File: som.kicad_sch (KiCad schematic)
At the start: 31 parts, among them M2 jetson-orin-nx/nano-module

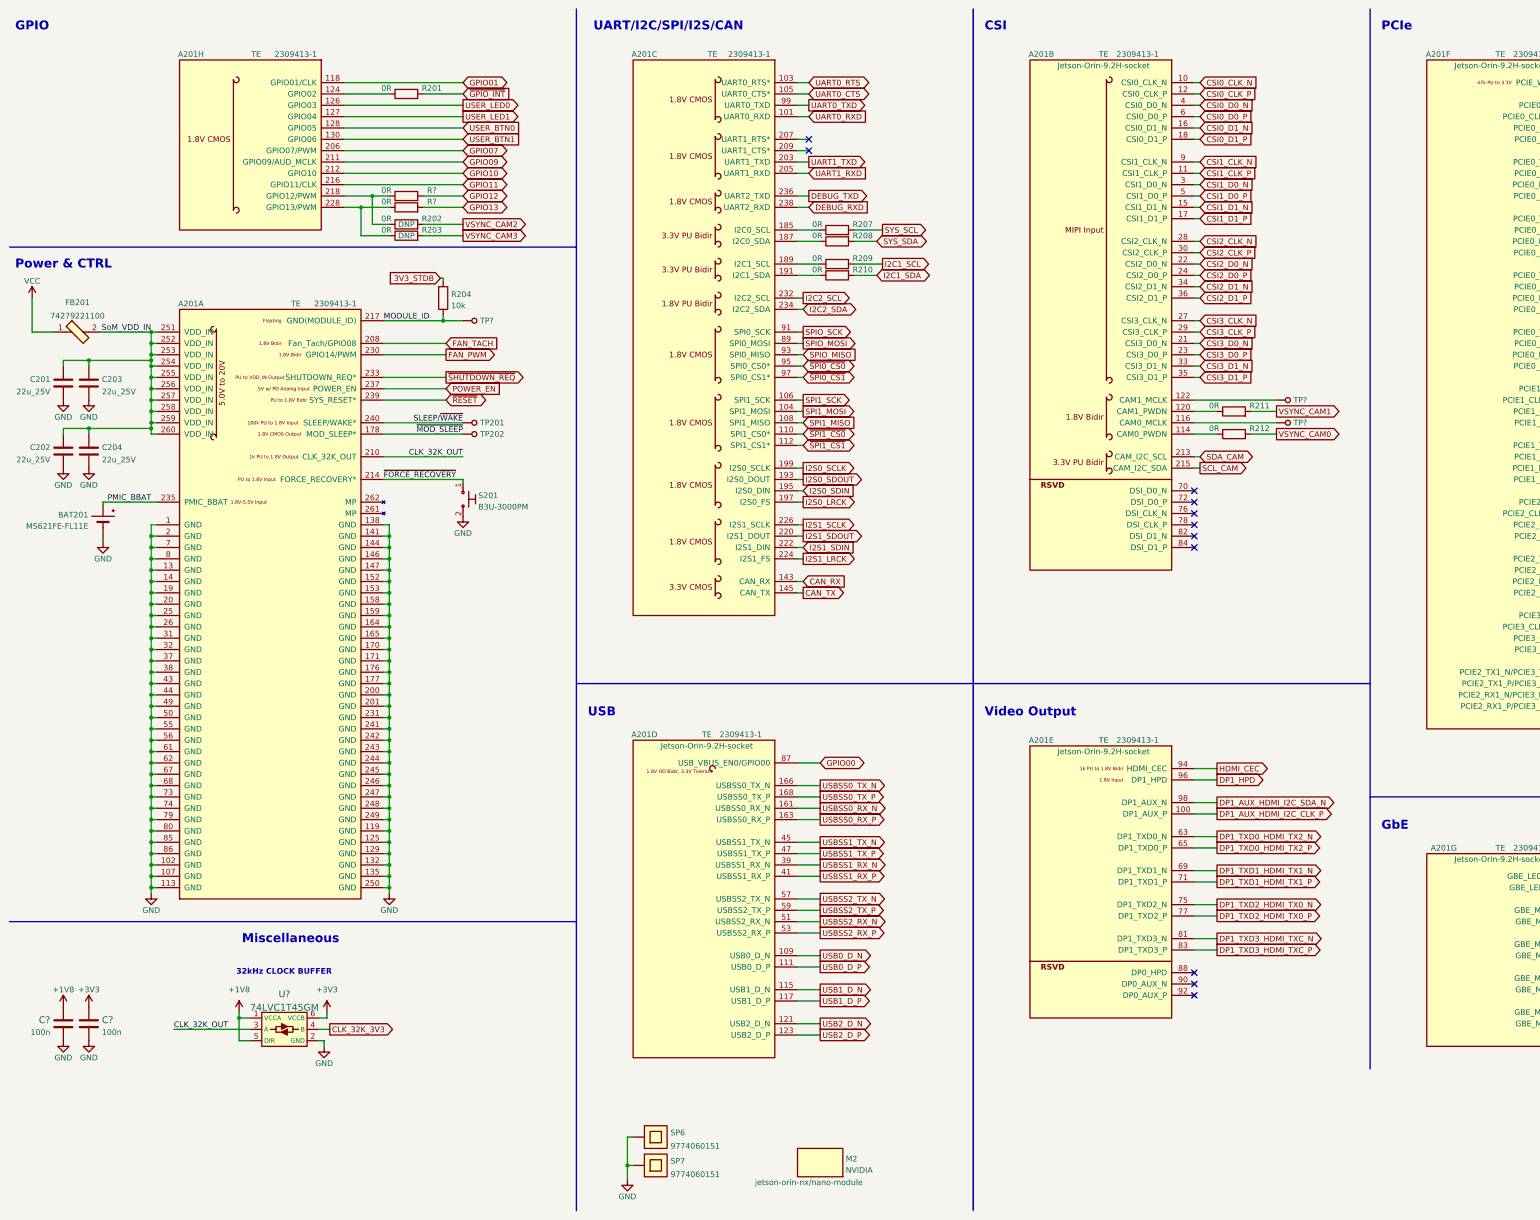
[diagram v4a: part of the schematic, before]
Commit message: Reannotate parts
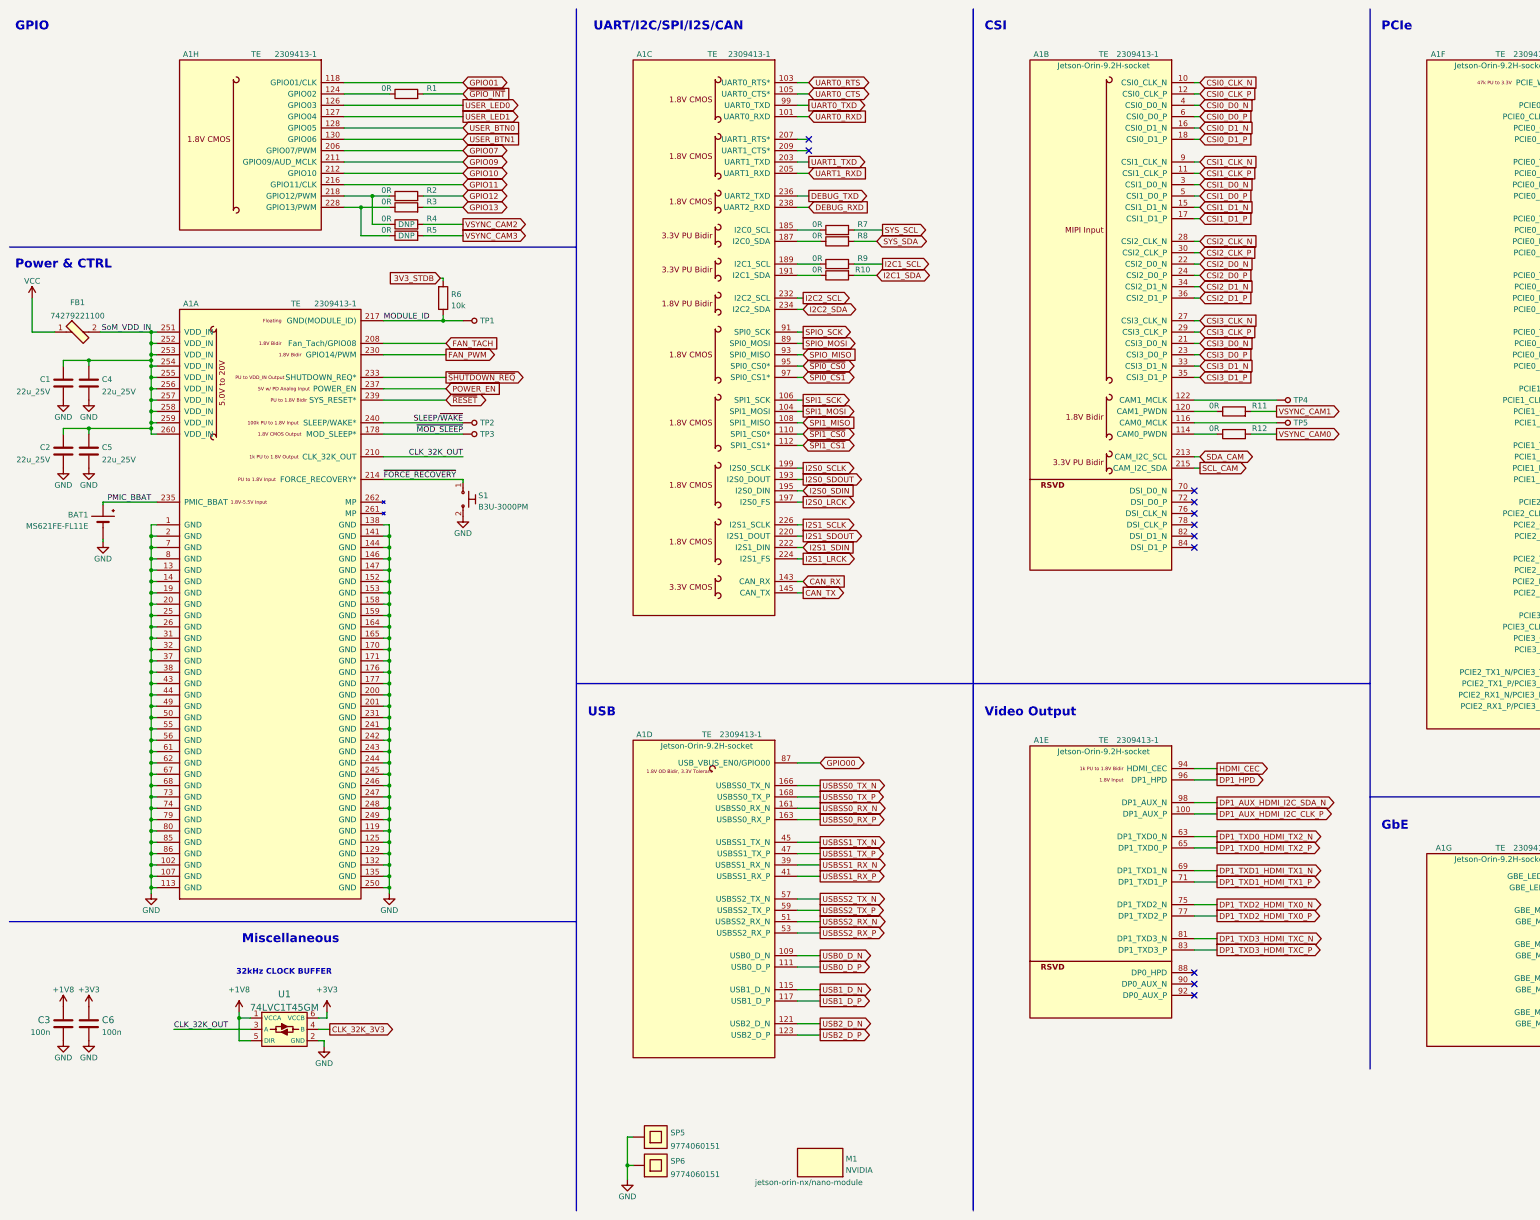
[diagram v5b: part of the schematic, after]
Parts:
- gave numbers to parts that had none: 8
- renumbered A201 to A1, BAT201 to BAT1, C201 to C1, C202 to C2, C203 to C4, C204 to C5, FB201 to FB1, M2 to M1, R201 to R1, R210 to R10, R211 to R11, R212 to R12, R202 to R4, R203 to R5, R204 to R6, R207 to R7, R208 to R8, R209 to R9, S201 to S1, SP6 to SP5, SP7 to SP6, TP201 to TP2, TP202 to TP3

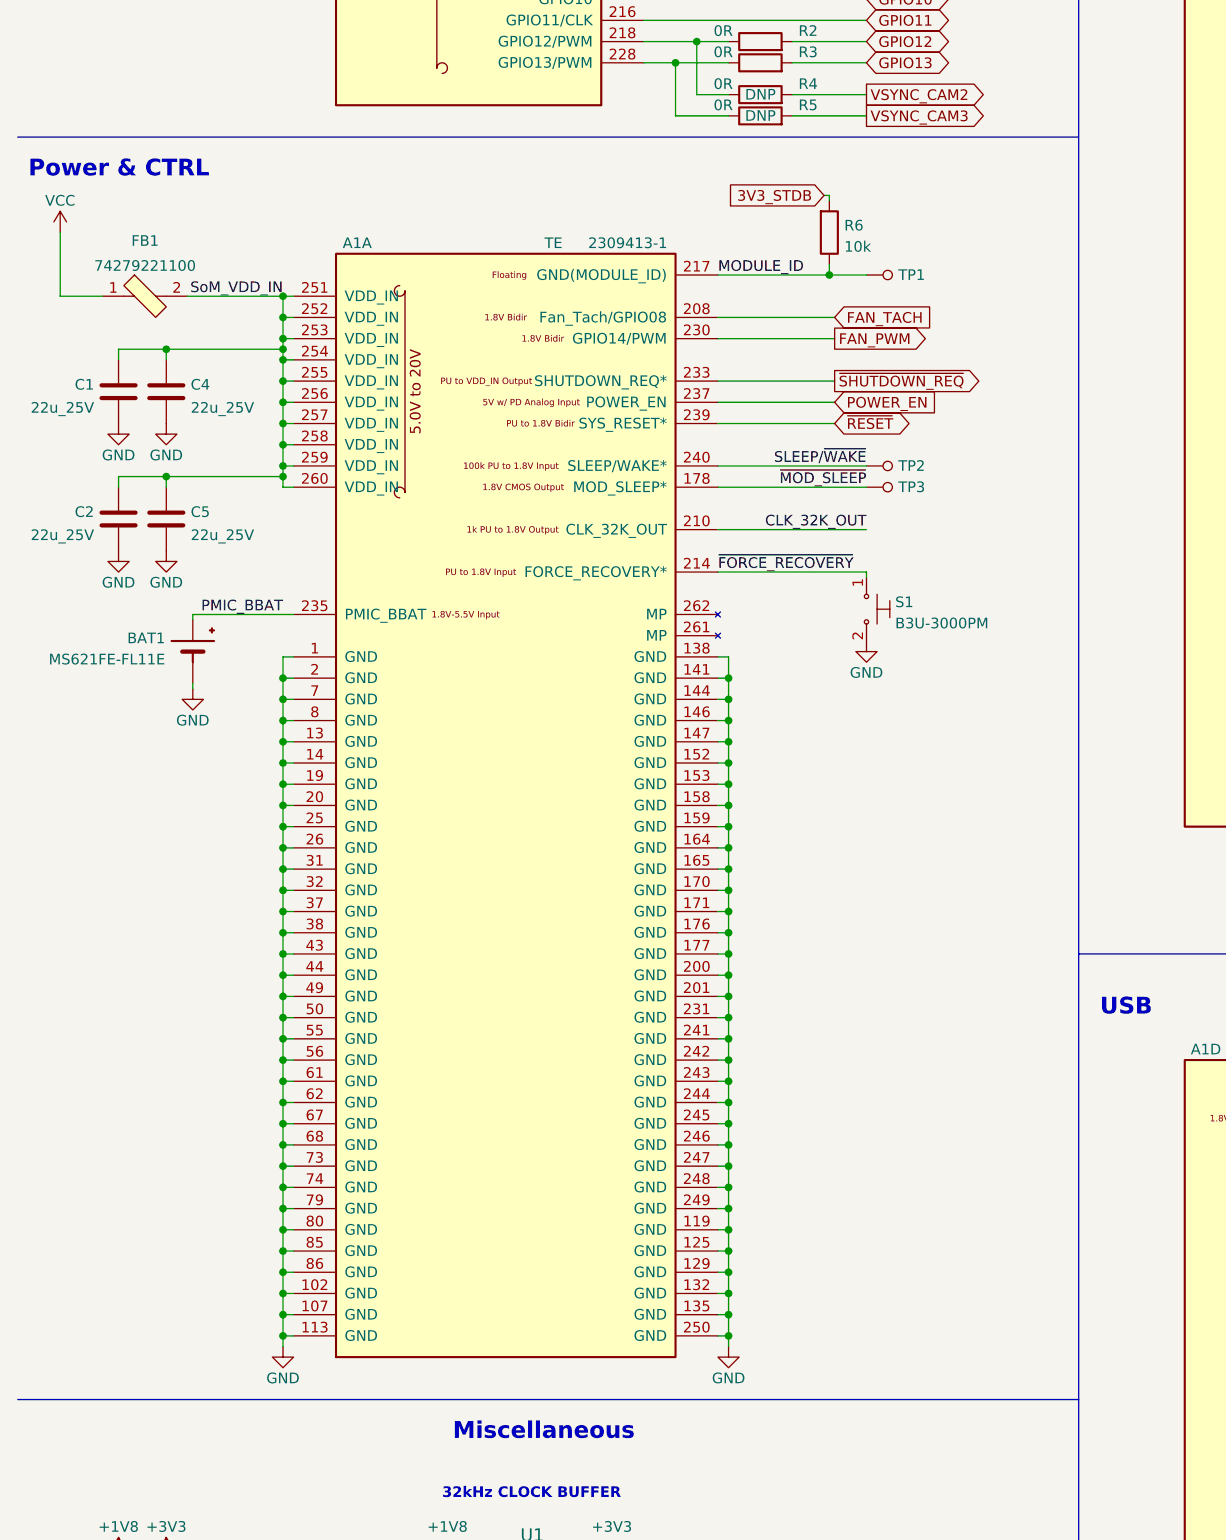
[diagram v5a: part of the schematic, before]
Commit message: Added RTC battery charge circuit
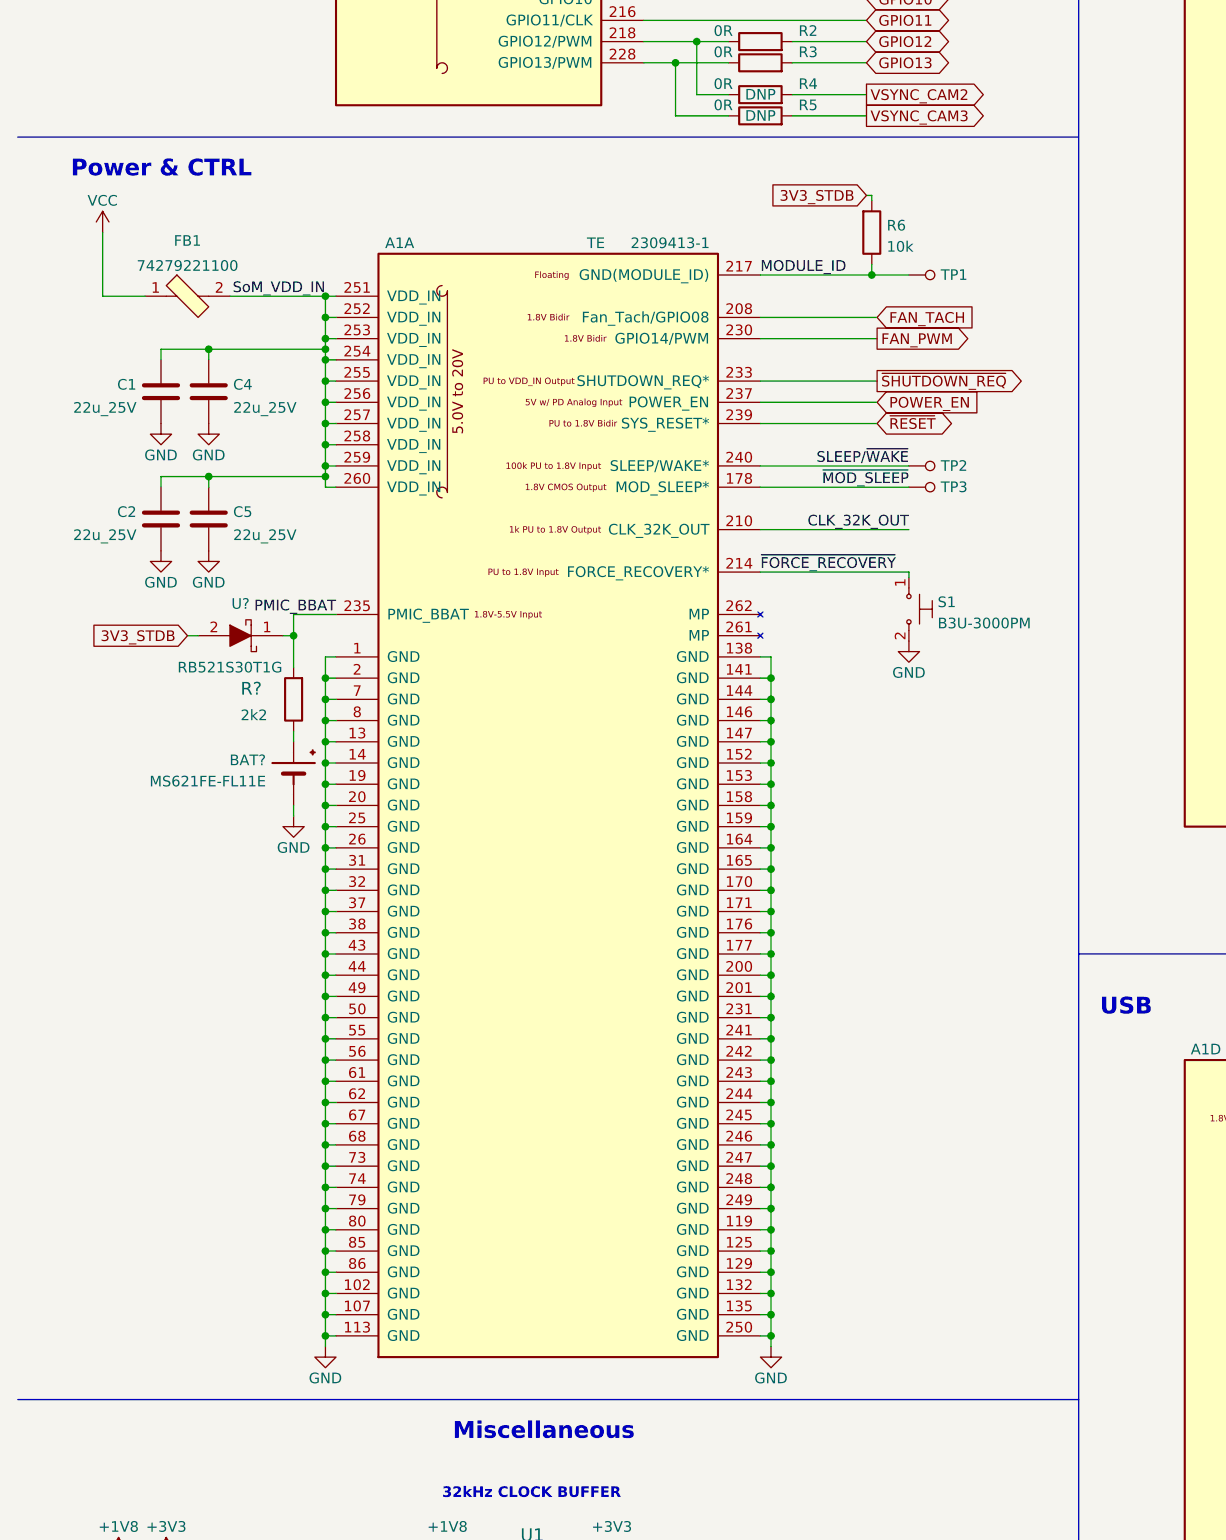
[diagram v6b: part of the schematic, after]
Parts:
- removed BAT1: MS621FE-FL11E, antmicro-footprints:MS621FE-FL11E, symbol antmicroBatteryHoldersClipsContacts:MS621FE-FL11E
- added BAT?: MS621FE-FL11E, antmicro-footprints:MS621FE-FL11E, symbol antmicroBatteryHoldersClipsContacts:MS621FE-FL11E
- added R?: R_2k2_0402, antmicro-footprints:0402-res, symbol antmicroResistors0402:R_2k2_0402
- added U?: RB521S30T1G, antmicro-footprints:SOD-523, symbol antmicroDiodesRectifiersSingle:RB521S30T1G
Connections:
- net 3V3_STDB: now also U?.2
- net GND: now also BAT?.-
- net PMIC_BBAT: now also R?.2, U?.1
- new net: BAT?.+, R?.1
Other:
- moved on the sheet: A1A, C1, C2, C4, C5, FB1, R6, S1, TP1, TP2, TP3
